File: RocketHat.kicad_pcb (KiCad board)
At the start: 2 copper layers, 68.3 x 58.8 mm, 28 parts, among them J1 Conn_01x06_Female, J10 Conn_01x10_Female, J11 Raspberry_Pi_2_3, J2 Conn_01x06_Female, J3 Conn_01x07_Female, J4 Conn_01x06_Female, J5 Conn_01x04_Female, J6 Conn_01x02_Female, J7 Conn_01x02, J8 Conn_01x10_Female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

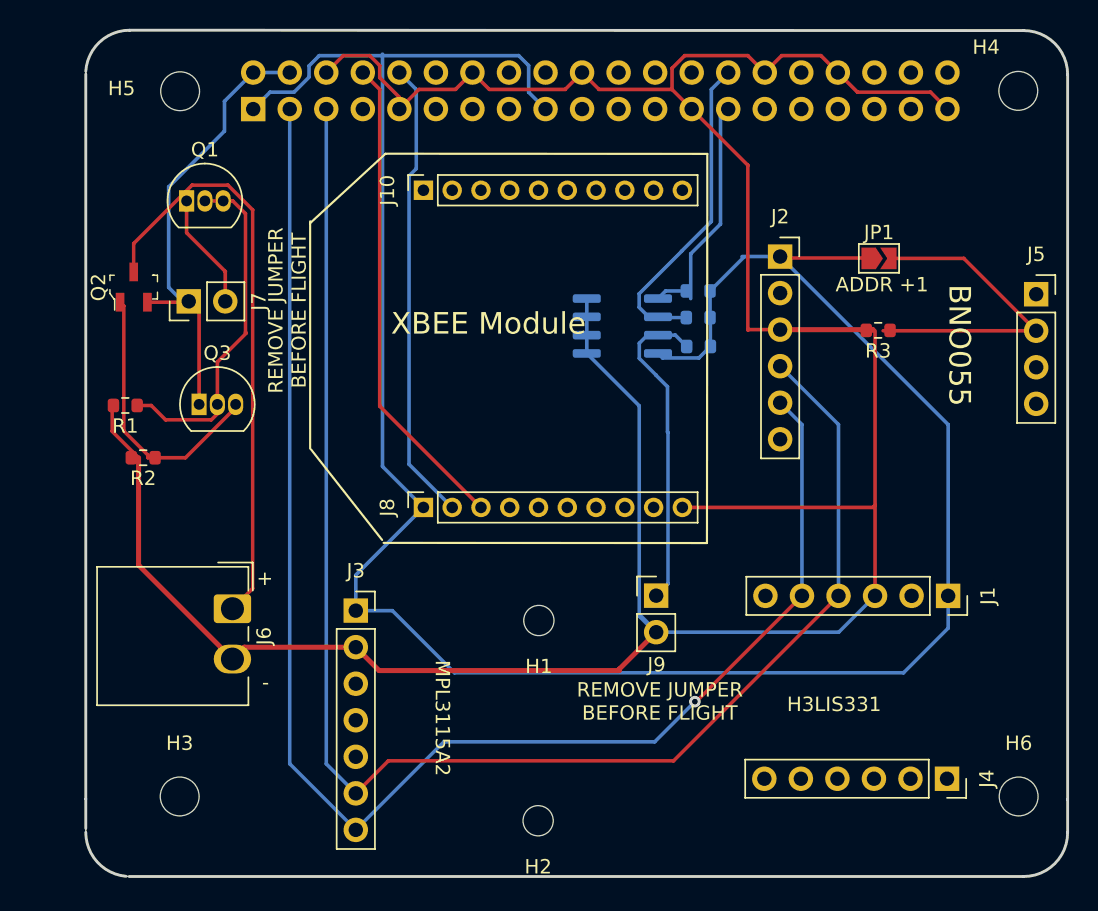
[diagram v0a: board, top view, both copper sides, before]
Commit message: Set Mounting Holes 1&2 to M2
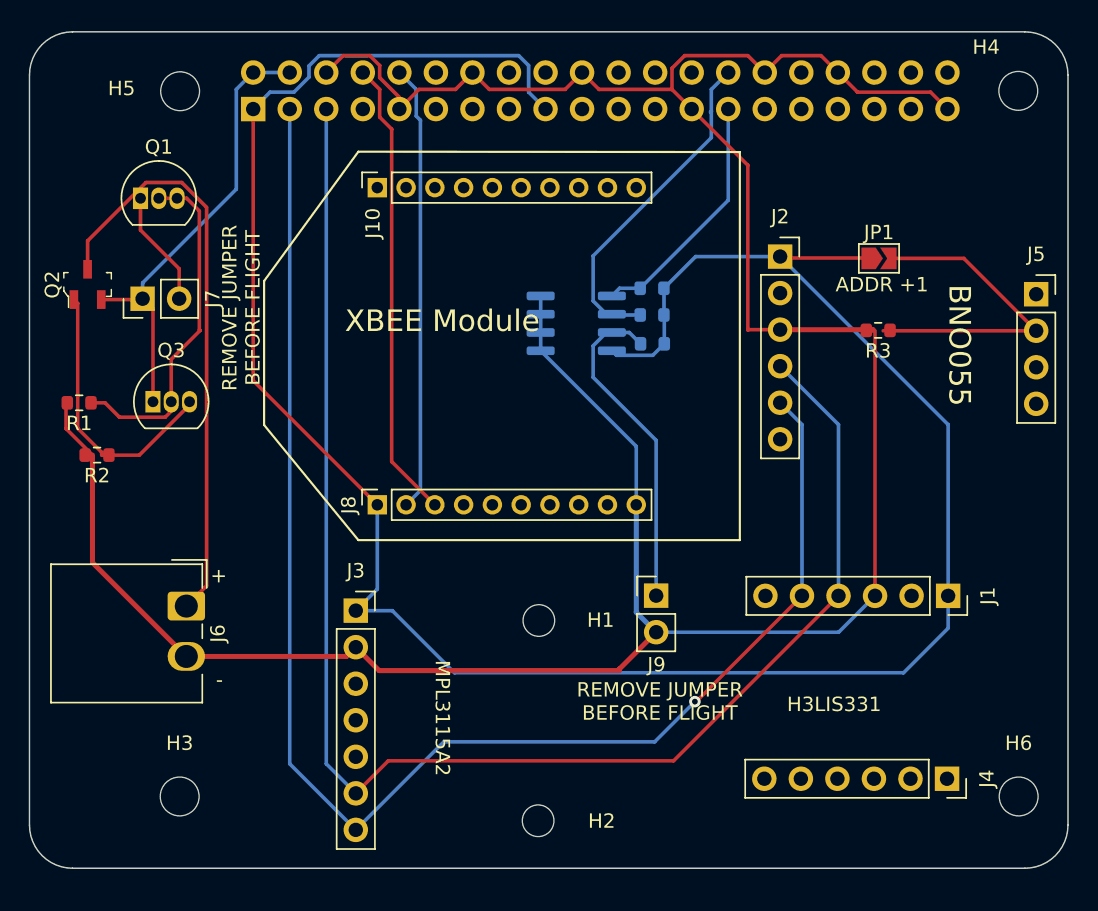
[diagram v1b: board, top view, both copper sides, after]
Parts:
- H1, H2: footprint MountingHole:MountingHole_2.1mm -> MountingHole:MountingHole_2.2mm_M2
- moved J6 3.21 mm to (207.9, 133.8)
- moved Q1 3.21 mm to (204.7, 105.4)
- moved R4 3.21 mm to (240.3, 115.5)
- moved R5 3.21 mm to (240.2, 111.7)
- moved R6 3.21 mm to (240.2, 113.5)
- moved U1 3.21 mm to (235.0, 114.1)
- moved J10 3.21 mm to (221.1, 104.7)
- moved J7 3.21 mm to (204.8, 112.4)
- moved J8 3.21 mm to (221.1, 126.7)
- moved Q2 3.21 mm to (201.0, 111.4)
- moved Q3 3.21 mm to (205.5, 119.6)
- moved R1 3.21 mm to (200.4, 119.6)
- moved R2 3.21 mm to (201.6, 123.3)
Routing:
- net GND: track 206.8 -> 197.9 mm
- net /EEPROM_SCL: track 21.7 -> 23.6 mm
- net /XBEE_RX: track 33.6 -> 32.1 mm
- net Net-(J9-Pad1): track 21.8 -> 23.2 mm
- net /XBEE_TX: track 32.2 -> 31.1 mm
- net /EEPROM_SDA: track 16.4 -> 17.2 mm
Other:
- board size 68.3 x 58.8 mm -> 72.2 x 58.1 mm

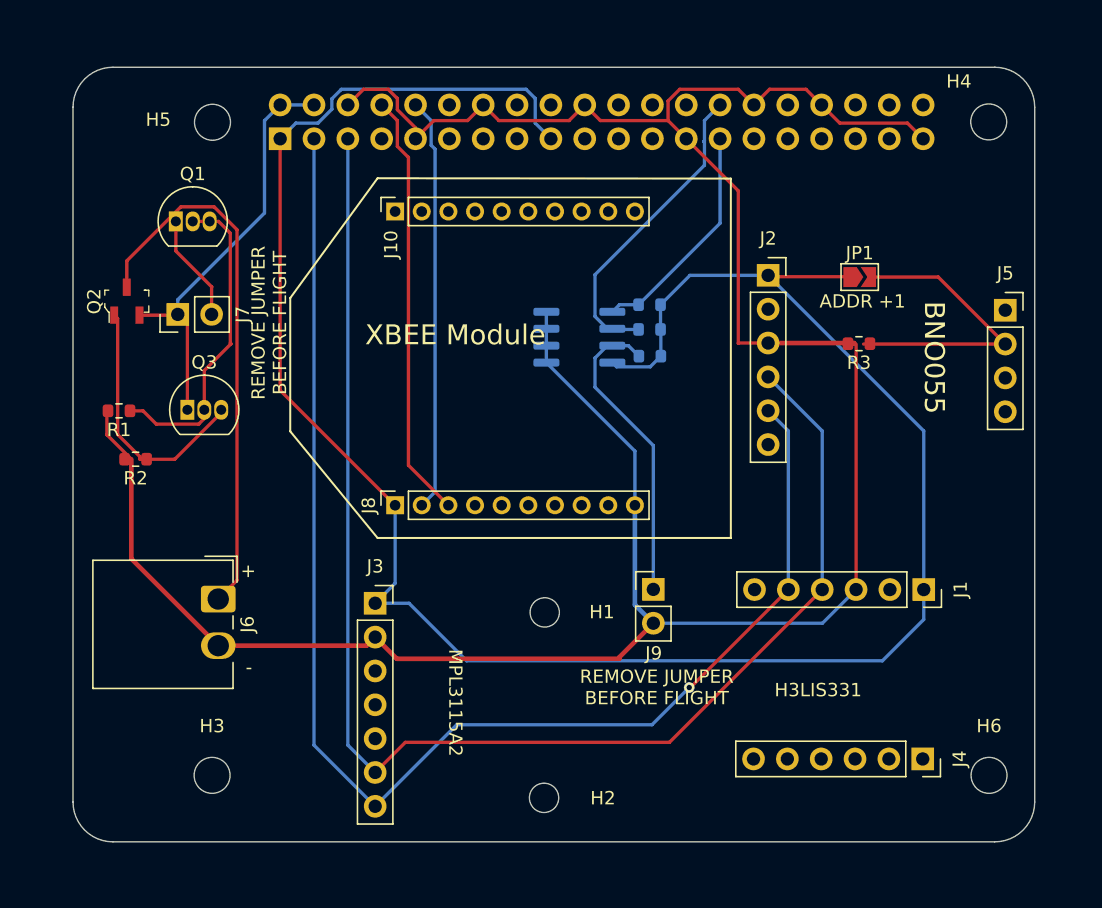
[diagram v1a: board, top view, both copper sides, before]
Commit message: Added Flood Zone
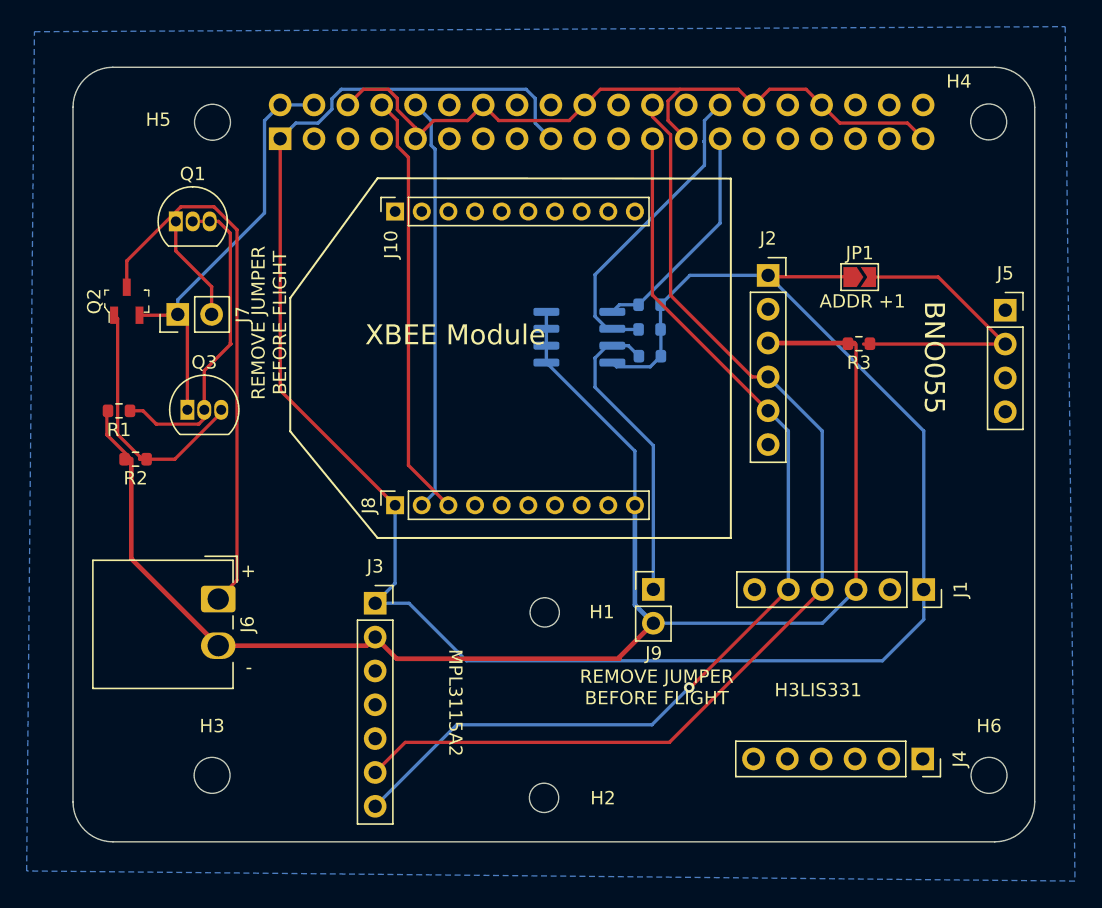
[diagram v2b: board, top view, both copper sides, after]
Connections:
- J11 pad 23: unconnected-(J11-Pad23) -> /SENSOR_SDA
- J11 pad 24: unconnected-(J11-Pad24) -> /SENSOR_SCL
- J11 pad 3: /SENSOR_SDA -> unconnected-(J11-Pad3)
- J11 pad 5: /SENSOR_SCL -> unconnected-(J11-Pad5)
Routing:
- net /SENSOR_SDA: track 103.8 -> 75.8 mm
- net /SENSOR_SCL: track 105.3 -> 81.6 mm
- net GND: track 197.9 -> 179.6 mm
- added copper zone on B.Cu, net GND
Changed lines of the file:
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@@
   (net 54 "unconnected-(J11-Pad29)")
   (net 55 "unconnected-(J11-Pad26)")
-  (net 56 "unconnected-(J11-Pad24)")
-  (net 57 "unconnected-(J11-Pad23)")
+  (net 56 "unconnected-(J11-Pad3)")
+  (net 57 "unconnected-(J11-Pad5)")
   (net 58 "unconnected-(J11-Pad22)")
   (net 59 "unconnected-(J11-Pad21)")
@@
       (net 2 "/P5V_HAT") (pinfunction "5V") (pintype "power_in"))
     (pad "3" thru_hole oval locked (at 0 -2.54 270) (size 1.7 1.7) (drill 1) (layers *.Cu *.Mask)
-      (net 9 "/SENSOR_SDA") (pinfunction "SDA/GPIO2") (pintype "bidirectional"))
+      (net 56 "unconnected-(J11-Pad3)") (pinfunction "SDA/GPIO2") (pintype "bidirectional"))
     (pad "4" thru_hole oval locked (at -2.54 -2.54 270) (size 1.7 1.7) (drill 1) (layers *.Cu *.Mask)
       (net 2 "/P5V_HAT") (pinfunction "5V") (pintype "power_in"))
     (pad "5" thru_hole oval locked (at 0 -5.08 270) (size 1.7 1.7) (drill 1) (layers *.Cu *.Mask)
-      (net 10 "/SENSOR_SCL") (pinfunction "SCL/GPIO3") (pintype "bidirectional"))
+      (net 57 "unconnected-(J11-Pad5)") (pinfunction "SCL/GPIO3") (pintype "bidirectional"))
     (pad "6" thru_hole oval locked (at -2.54 -5.08 270) (size 1.7 1.7) (drill 1) (layers *.Cu *.Mask)
       (net 5 "GND") (pinfunction "GND") (pintype "power_in"))
@@
       (net 58 "unconnected-(J11-Pad22)") (pinfunction "GPIO25") (pintype "bidirectional"))
     (pad "23" thru_hole oval locked (at 0 -27.94 270) (size 1.7 1.7) (drill 1) (layers *.Cu *.Mask)
-      (net 57 "unconnected-(J11-Pad23)") (pinfunction "SCLK0/GPIO11") (pintype "bidirectional"))
+      (net 9 "/SENSOR_SDA") (pinfunction "SCLK0/GPIO11") (pintype "bidirectional"))
     (pad "24" thru_hole oval locked (at -2.54 -27.94 270) (size 1.7 1.7) (drill 1) (layers *.Cu *.Mask)
-      (net 56 "unconnected-(J11-Pad24)") (pinfunction "~{CE0}/GPIO8") (pintype "bidirectional"))
+      (net 10 "/SENSOR_SCL") (pinfunction "~{CE0}/GPIO8") (pintype "bidirectional"))
     (pad "25" thru_hole oval locked (at 0 -30.48 270) (size 1.7 1.7) (drill 1) (layers *.Cu *.Mask)
       (net 5 "GND") (pinfunction "GND") (pintype "power_in"))
@@
   (segment (start 235.361744 96.680944) (end 234.187233 97.855455) (width 0.25) (layer "F.Cu") (net 5))
   (segment (start 218.9896 137.27) (end 219.6334 136.6262) (width 0.35) (layer "F.Cu") (net 5))
-  (segment (start 246.888 114.5794) (end 246.9134 114.554) (width 0.25) (layer "F.Cu") (net 5))
   (segment (start 255.727944 133.059144) (end 255.727944 114.638744) (width 0.25) (layer "F.Cu") (net 5))
   (segment (start 259.587233 98.046433) (end 260.761744 99.220944) (width 0.25) (layer "F.Cu") (net 5))
   (segment (start 218.756255 95.506433) (end 217.581744 96.680944) (width 0.25) (layer "F.Cu") (net 5))
   (segment (start 240.5126 135.5852) (end 237.9472 138.1506) (width 0.35) (layer "F.Cu") (net 5))
+  (segment (start 236.536255 95.506433) (end 246.887233 95.506433) (width 0.25) (layer "F.Cu") (net 5))
   (segment (start 199.49218 121.43722) (end 199.49218 119.64212) (width 0.25) (layer "F.Cu") (net 5))
   (segment (start 249.129 114.554) (end 255.5752 114.554) (width 0.35) (layer "F.Cu") (net 5))
   (segment (start 246.887233 95.506433) (end 248.061744 96.680944) (width 0.25) (layer "F.Cu") (net 5))
   (segment (start 248.061744 96.680944) (end 249.236255 95.506433) (width 0.25) (layer "F.Cu") (net 5))
-  (segment (start 246.888 103.1272) (end 246.888 114.5794) (width 0.25) (layer "F.Cu") (net 5))
-  (segment (start 242.495245 95.506433) (end 246.887233 95.506433) (width 0.25) (layer "F.Cu") (net 5))
   (segment (start 221.296255 97.039455) (end 221.296255 96.194445) (width 0.25) (layer "F.Cu") (net 5))
   (segment (start 242.981744 99.220944) (end 241.616255 97.855455) (width 0.25) (layer "F.Cu") (net 5))
@@
   (segment (start 207.8534 137.27) (end 201.32928 130.74588) (width 0.35) (layer "F.Cu") (net 5))
   (segment (start 249.236255 95.506433) (end 251.967233 95.506433) (width 0.25) (layer "F.Cu") (net 5))
-  (segment (start 241.616255 97.855455) (end 236.536255 97.855455) (width 0.25) (layer "F.Cu") (net 5))
   (segment (start 241.616255 97.855455) (end 241.616255 96.385423) (width 0.25) (layer "F.Cu") (net 5))
   (segment (start 224.027233 97.855455) (end 222.661744 99.220944) (width 0.25) (layer "F.Cu") (net 5))
-  (segment (start 246.9134 114.554) (end 249.129 114.554) (width 0.25) (layer "F.Cu") (net 5))
   (segment (start 220.608243 95.506433) (end 218.756255 95.506433) (width 0.25) (layer "F.Cu") (net 5))
   (segment (start 201.32928 130.74588) (end 201.32928 123.27432) (width 0.35) (layer "F.Cu") (net 5))
@@
   (segment (start 255.5752 114.554) (end 255.624544 114.603344) (width 0.35) (layer "F.Cu") (net 5))
   (segment (start 237.9472 138.1506) (end 237.9472 138.2522) (width 0.35) (layer "F.Cu") (net 5))
-  (segment (start 242.981744 99.220944) (end 246.888 103.1272) (width 0.25) (layer "F.Cu") (net 5))
   (segment (start 227.741744 96.680944) (end 226.567233 97.855455) (width 0.25) (layer "F.Cu") (net 5))
   (segment (start 222.661744 98.404944) (end 221.296255 97.039455) (width 0.25) (layer "F.Cu") (net 5))
-  (segment (start 236.536255 97.855455) (end 235.361744 96.680944) (width 0.25) (layer "F.Cu") (net 5))
   (segment (start 222.661744 99.220944) (end 222.661744 98.404944) (width 0.25) (layer "F.Cu") (net 5))
   (segment (start 221.2594 138.2522) (end 237.9472 138.2522) (width 0.35) (layer "F.Cu") (net 5))
+  (segment (start 235.361744 96.680944) (end 236.536255 95.506433) (width 0.25) (layer "F.Cu") (net 5))
   (segment (start 241.616255 96.385423) (end 242.495245 95.506433) (width 0.25) (layer "F.Cu") (net 5))
   (segment (start 239.1288 122.6668) (end 239.1288 126.7292) (width 0.25) (layer "B.Cu") (net 5))
@@
   (segment (start 243.205 140.4112) (end 243.295888 140.4112) (width 0.25) (layer "F.Cu") (net 9))
   (segment (start 243.295888 140.4112) (end 250.647944 133.059144) (width 0.25) (layer "F.Cu") (net 9))
+  (segment (start 240.441744 99.220944) (end 240.441744 110.946744) (width 0.25) (layer "F.Cu") (net 9))
+  (segment (start 240.441744 110.946744) (end 249.129 119.634) (width 0.25) (layer "F.Cu") (net 9))
   (via (at 243.205 140.4112) (size 0.8) (drill 0.4) (layers "F.Cu" "B.Cu") (net 9))
-  (segment (start 215.041744 144.734544) (end 219.6334 149.3262) (width 0.25) (layer "B.Cu") (net 9))
   (segment (start 250.647944 133.059144) (end 250.647944 121.152944) (width 0.25) (layer "B.Cu") (net 9))
-  (segment (start 215.041744 99.220944) (end 215.041744 144.734544) (width 0.25) (layer "B.Cu") (net 9))
   (segment (start 219.6334 149.3262) (end 225.7544 143.2052) (width 0.25) (layer "B.Cu") (net 9))
   (segment (start 240.411 143.2052) (end 243.205 140.4112) (width 0.25) (layer "B.Cu") (net 9))
@@
   (segment (start 219.6334 146.7862) (end 221.8936 144.526) (width 0.25) (layer "F.Cu") (net 10))
   (segment (start 221.8936 144.526) (end 241.721088 144.526) (width 0.25) (layer "F.Cu") (net 10))
+  (segment (start 241.807233 110.974314) (end 247.926919 117.094) (width 0.25) (layer "F.Cu") (net 10))
+  (segment (start 247.926919 117.094) (end 249.129 117.094) (width 0.25) (layer "F.Cu") (net 10))
+  (segment (start 240.441744 96.680944) (end 240.441744 97.559934) (width 0.25) (layer "F.Cu") (net 10))
+  (segment (start 240.441744 97.559934) (end 241.807233 98.925423) (width 0.25) (layer "F.Cu") (net 10))
   (segment (start 241.721088 144.526) (end 253.187944 133.059144) (width 0.25) (layer "F.Cu") (net 10))
-  (segment (start 217.581744 144.734544) (end 217.581744 99.220944) (width 0.25) (layer "B.Cu") (net 10))
-  (segment (start 219.6334 146.7862) (end 217.581744 144.734544) (width 0.25) (layer "B.Cu") (net 10))
+  (segment (start 241.807233 98.925423) (end 241.807233 110.974314) (width 0.25) (layer "F.Cu") (net 10))
   (segment (start 249.129 117.094) (end 253.187944 121.152944) (width 0.25) (layer "B.Cu") (net 10))
   (segment (start 253.187944 121.152944) (end 253.187944 133.059144) (width 0.25) (layer "B.Cu") (net 10))
@@
   (segment (start 224.128311 125.729689) (end 224.128311 99.999499) (width 0.25) (layer "B.Cu") (net 13))
   (segment (start 236.134336 117.871936) (end 240.5126 122.2502) (width 0.25) (layer "B.Cu") (net 19))
-  (segment (start 237.433856 114.751856) (end 237.057784 114.751856) (width 0.25) (layer "B.Cu") (net 19))
   (segment (start 238.640856 114.751856) (end 237.433856 114.751856) (width 0.25) (layer "B.Cu") (net 19))
   (segment (start 236.134336 115.675304) (end 236.134336 117.871936) (width 0.25) (layer "B.Cu") (net 19))
@@
   (segment (start 237.057784 113.481856) (end 236.134336 112.558408) (width 0.25) (layer "B.Cu") (net 27))
   (segment (start 236.134336 109.420288) (end 244.348 101.206624) (width 0.25) (layer "B.Cu") (net 27))
-  (segment (start 237.433856 113.481856) (end 237.057784 113.481856) (width 0.25) (layer "B.Cu") (net 27))
+  (zone (net 5) (net_name "GND") (layer "B.Cu") (hatch edge 0.508)
+    (connect_pads (clearance 0.508))
+    (min_thickness 0.254) (filled_areas_thickness no)
+    (fill yes (thermal_gap 0.508) (thermal_bridge_width 0.508))
+    (polygon
+      (pts
+        (xy 272.161 154.94)
+        (xy 193.4718 154.178)
+        (xy 194.056 91.186)
+        (xy 271.4244 90.805)
+      )
+    )
+  )
   (group "group-boardCharacteristics" (id 05af41ed-4d28-4bb8-96c8-0afae8ed9738)
     (members

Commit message: Smol Board
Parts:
- moved H2 170.2 mm to (77.5, 78.0)
- moved H3 170.2 mm to (52.5, 76.4)
- moved H4 170.2 mm to (110.8, 27.3)
- moved H6 170.2 mm to (110.9, 76.4)
- moved J1 170.2 mm to (106.0, 62.4)
- moved J10 170.2 mm to (66.3, 34.0)
- moved J5 170.2 mm to (112.1, 41.4)
- moved J8 170.2 mm to (66.3, 56.1)
- moved JP1 170.2 mm to (101.2, 38.9)
- moved Q2 170.2 mm to (46.1, 40.8)
- moved R1 170.2 mm to (45.6, 49.0)
- moved R3 170.2 mm to (101.1, 43.9)
- moved H1 170.2 mm to (77.5, 64.1)
- moved H5 170.2 mm to (52.6, 27.3)
- moved J11 170.2 mm to (57.7, 28.6)
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
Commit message: Even SMOLLER Board
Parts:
- moved H1 30.2 mm to (48.9, 54.3)
- moved R5 30.2 mm to (56.8, 31.2)
- moved R6 30.2 mm to (56.8, 33.0)
- moved H4 30.2 mm to (82.3, 17.4)
- moved H5 30.2 mm to (24.0, 17.5)
- moved J1 30.2 mm to (77.4, 52.5)
- moved J10 30.2 mm to (37.7, 24.2)
- moved J11 30.2 mm to (29.1, 18.7)
- moved J2 30.2 mm to (65.7, 29.0)
- moved J5 30.2 mm to (83.5, 31.6)
- moved J7 30.2 mm to (21.4, 31.9)
- moved Q1 30.2 mm to (21.3, 24.9)
- moved Q2 30.2 mm to (17.6, 30.9)
- moved R2 30.2 mm to (18.2, 42.8)
- moved J6 30.2 mm to (24.4, 53.2)
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
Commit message: Smol Board + Title Block
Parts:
- moved H4 97.9 mm to (179.0, 32.6)
- moved J1 97.9 mm to (174.1, 67.7)
- moved J2 97.9 mm to (162.4, 44.1)
- moved J3 97.9 mm to (132.9, 68.7)
- moved J4 97.9 mm to (174.0, 80.4)
- moved JP1 97.9 mm to (169.3, 44.2)
- moved R4 97.9 mm to (153.5, 50.2)
- moved U1 97.9 mm to (148.2, 48.8)
- moved H1 97.9 mm to (145.6, 69.4)
- moved H2 97.9 mm to (145.6, 83.3)
- moved H3 97.9 mm to (120.7, 81.6)
- moved H5 97.9 mm to (120.7, 32.6)
- moved H6 97.9 mm to (179.0, 81.6)
- moved J10 97.9 mm to (134.4, 39.3)
- moved J11 97.9 mm to (125.8, 33.9)
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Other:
- board text added: "Version 1.0"
